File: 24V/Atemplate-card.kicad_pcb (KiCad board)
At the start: 2 copper layers, 111.8 x 83 mm, 8 parts, among them J1 Conn_01x10_Pin

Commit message: JLC Design Constraints
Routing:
- net GND2: vias 251 -> 252
- net /48v: vias 136 -> 116

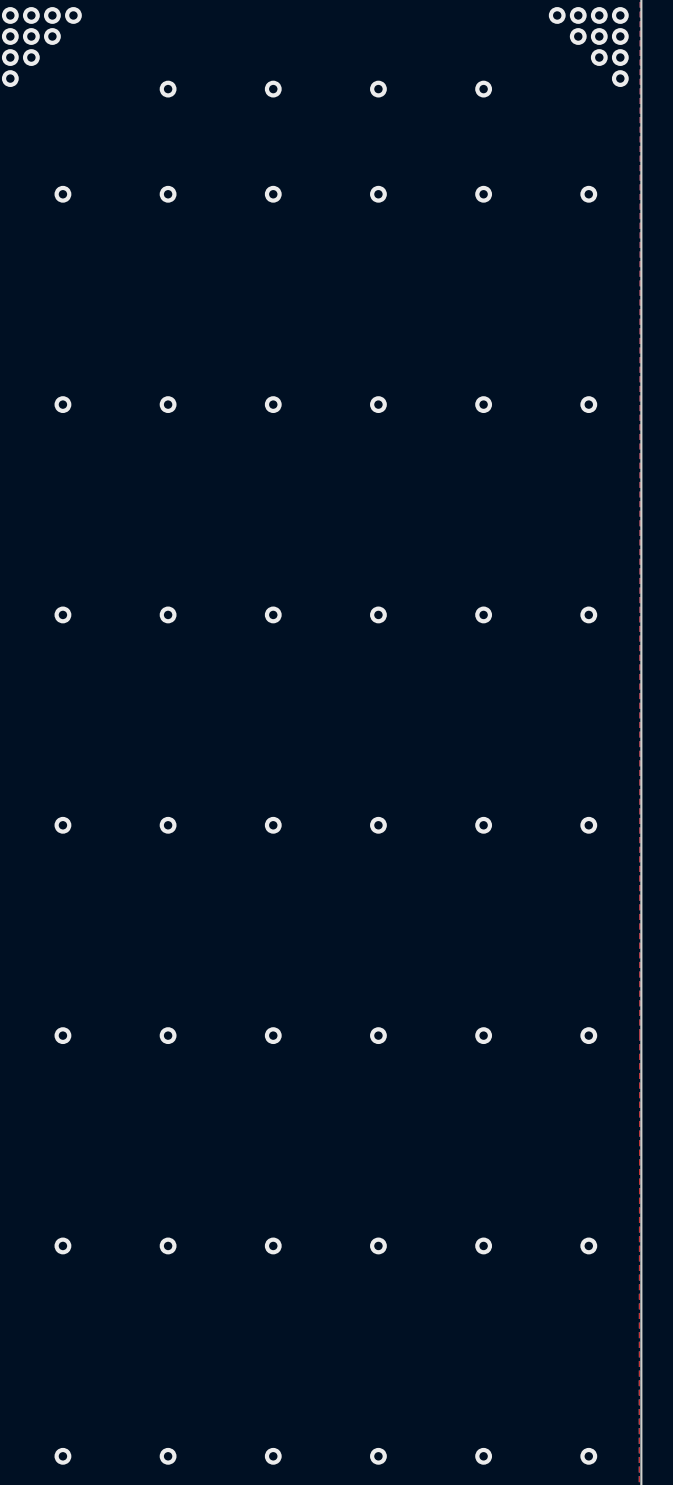
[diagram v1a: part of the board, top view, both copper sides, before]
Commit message: Bus silkscreens
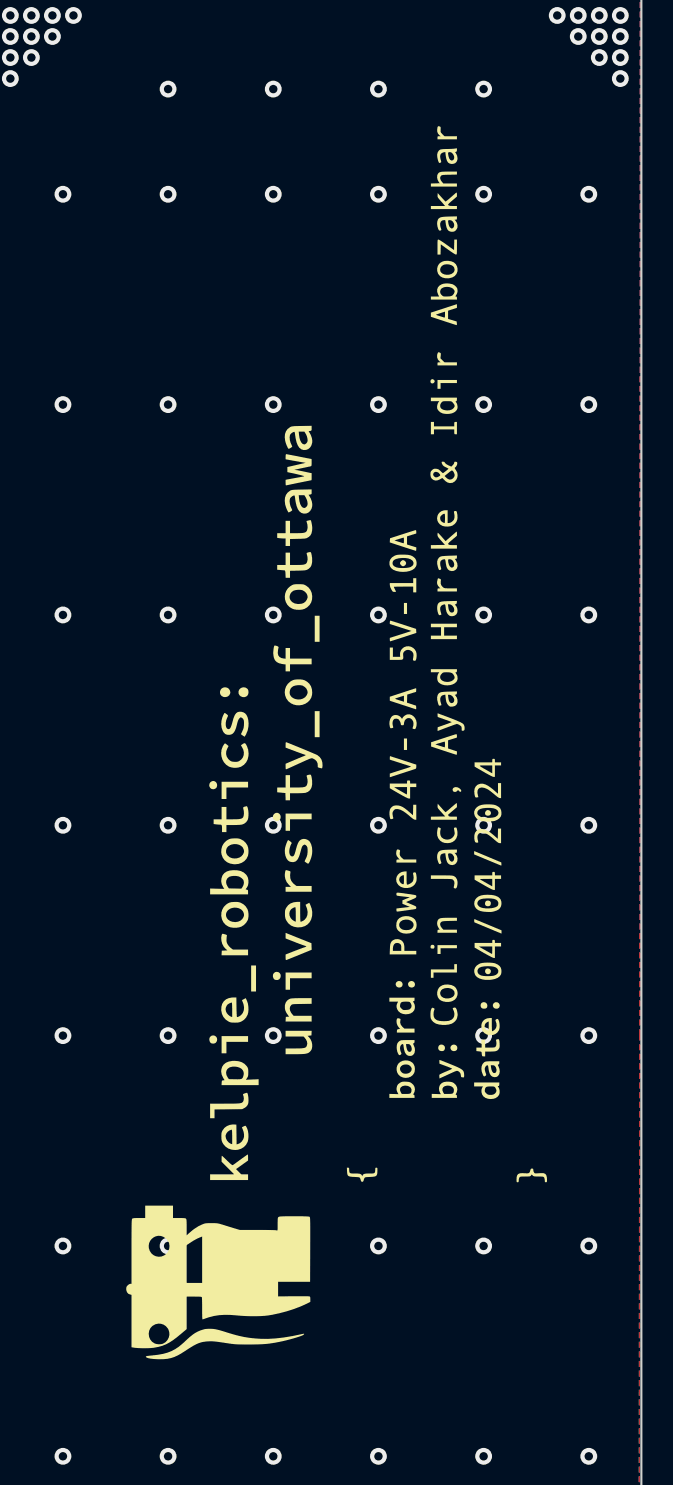
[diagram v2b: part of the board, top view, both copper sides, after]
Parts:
- added G***: LOGO, silks:24VBoard, F.Cu at (183.0, 61.0)
